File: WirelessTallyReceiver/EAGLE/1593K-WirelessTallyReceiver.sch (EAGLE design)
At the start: 8 parts, among them J2 POWER_JACK

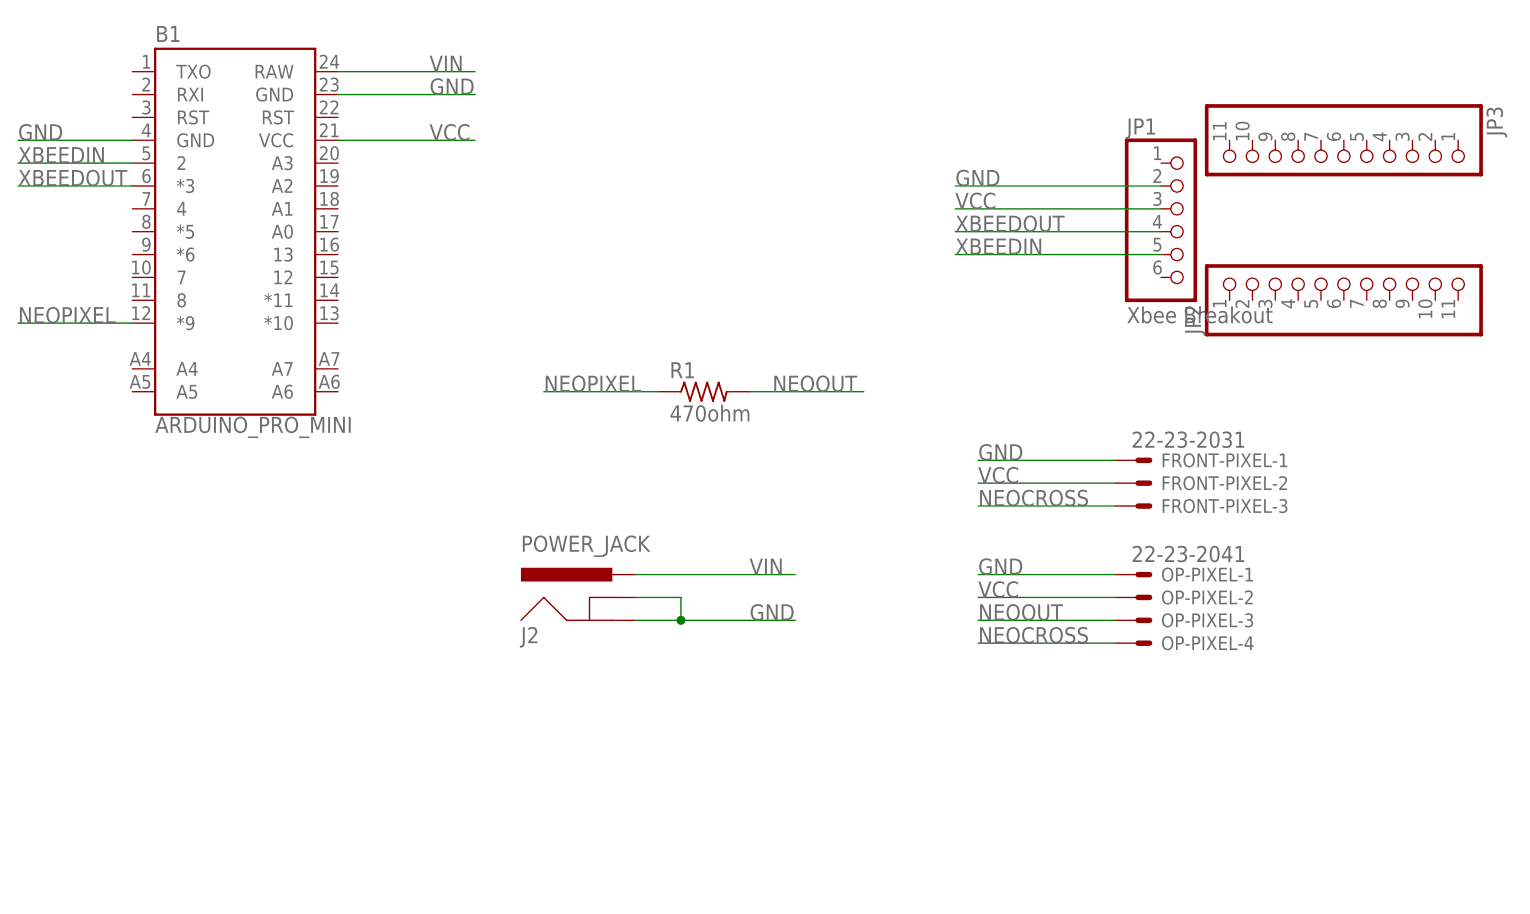
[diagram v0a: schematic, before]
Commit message: Revisions to boards after working with initial prototypes.
- Update boards to use SMD components to help save on space.
- Redesign wireless receiver to use 3.3v logic to avoid using the Xbee breakout.
- Remove designs that aren't going to be used.
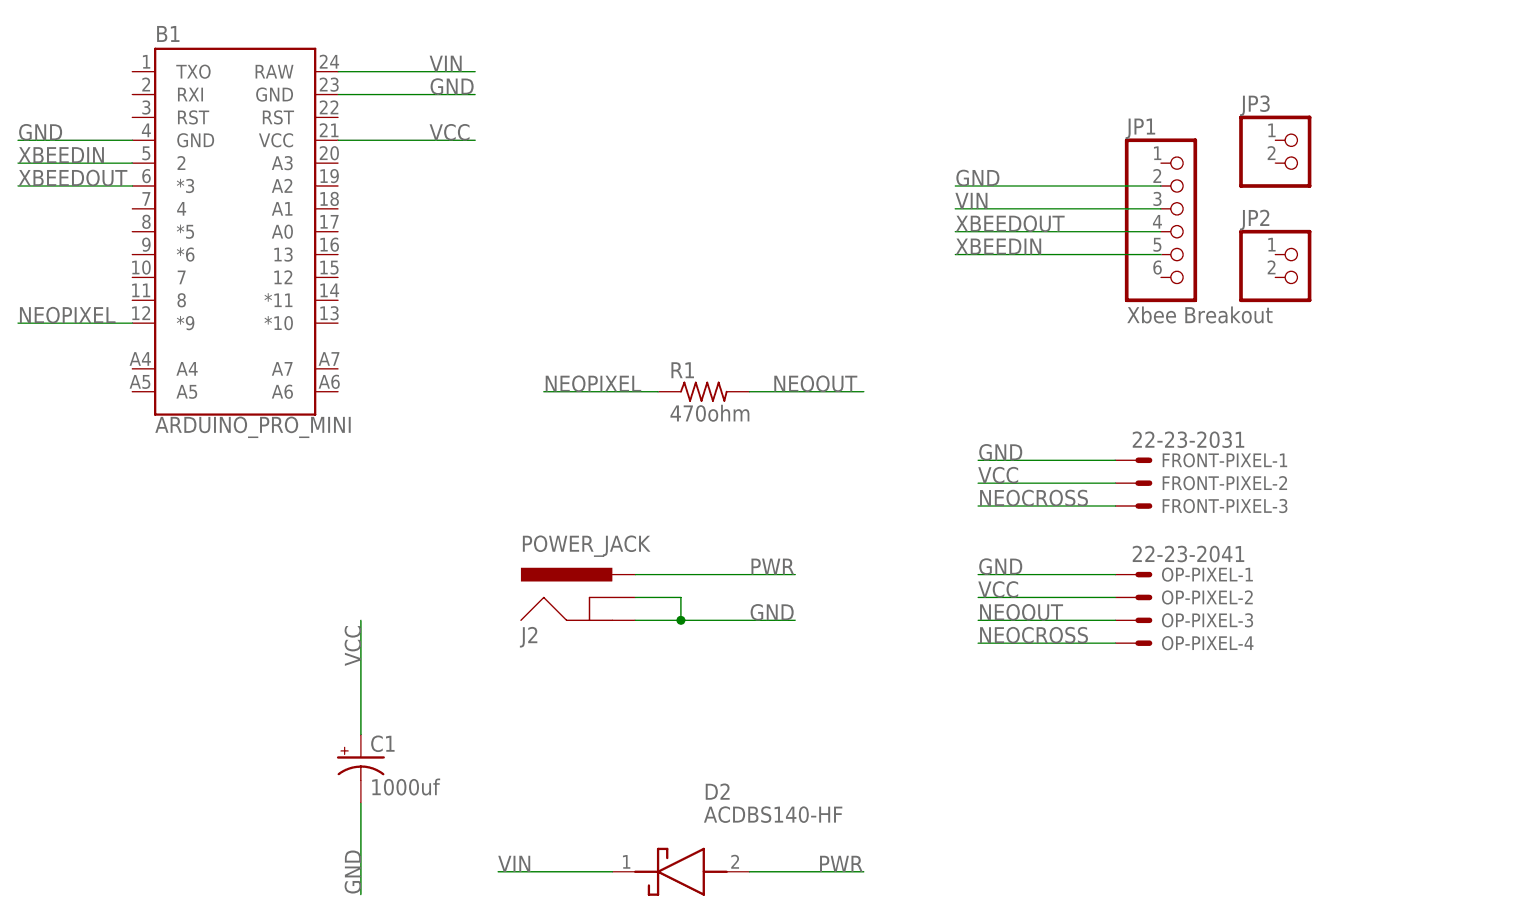
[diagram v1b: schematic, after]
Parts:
- added C1: 1000uf, SparkFun-Capacitors:1000UF-RADIAL-5MM-25V-20%
- added D2: ACDBS140-HF, SamacSys_Parts:ACDBS140-HF
- JP2, JP3: device pinhead:PINHD-1X11 -> pinhead:PINHD-1X2
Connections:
- new net PWR: D2.A, J2.PWR
- net GND: now also C1.-
- net VCC: now also C1.+; no longer JP1.3
- net VIN: now also D2.K, JP1.3; no longer J2.PWR
